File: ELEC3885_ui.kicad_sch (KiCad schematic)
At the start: 0 parts

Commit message: Initial schematic complete
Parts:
- added SW1, SW2, SW3, SW4: SW_Push, Button_Switch_SMD:SW_Push_1P1T_NO_6x6mm_H9.5mm, symbol Switch:SW_Push_Dual
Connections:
- new net BUTTON_0: SW1.1, SW1.3
- new net BUTTON_1: SW2.1, SW2.3
- new net BUTTON_2: SW3.1, SW3.3
- new net BUTTON_3: SW4.1, SW4.3
- new net GND: SW1.2, SW1.4, SW2.2, SW2.4, SW3.2, SW3.4, SW4.2, SW4.4
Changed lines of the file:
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@@
 (kicad_sch (version 20211123) (generator eeschema)
   (paper "A4")
+  (junction (at 154.94 87.63) (diameter 0) (color 0 0 0 0)
+  )
+  (junction (at 154.94 57.15) (diameter 0) (color 0 0 0 0)
+  )
+  (junction (at 154.94 97.79) (diameter 0) (color 0 0 0 0)
+  )
+  (junction (at 137.16 97.79) (diameter 0) (color 0 0 0 0)
+  )
+  (junction (at 154.94 82.55) (diameter 0) (color 0 0 0 0)
+  )
+  (junction (at 137.16 82.55) (diameter 0) (color 0 0 0 0)
+  )
+  (junction (at 154.94 72.39) (diameter 0) (color 0 0 0 0)
+  )
+  (junction (at 154.94 102.87) (diameter 0) (color 0 0 0 0)
+  )
+  (junction (at 154.94 67.31) (diameter 0) (color 0 0 0 0)
+  )
+  (junction (at 137.16 67.31) (diameter 0) (color 0 0 0 0)
+  )
+  (junction (at 137.16 52.07) (diameter 0) (color 0 0 0 0)
+  )
+  (wire (pts (xy 137.16 97.79) (xy 137.16 102.87))
+    (stroke (width 0) (type default) (color 0 0 0 0))
+  )
+  (wire (pts (xy 128.27 82.55) (xy 137.16 82.55))
+    (stroke (width 0) (type default) (color 0 0 0 0))
+  )
+  (wire (pts (xy 137.16 82.55) (xy 137.16 87.63))
+    (stroke (width 0) (type default) (color 0 0 0 0))
+  )
+  (wire (pts (xy 154.94 97.79) (xy 154.94 102.87))
+    (stroke (width 0) (type default) (color 0 0 0 0))
+  )
+  (wire (pts (xy 154.94 67.31) (xy 154.94 72.39))
+    (stroke (width 0) (type default) (color 0 0 0 0))
+  )
+  (wire (pts (xy 128.27 97.79) (xy 137.16 97.79))
+    (stroke (width 0) (type default) (color 0 0 0 0))
+  )
+  (wire (pts (xy 154.94 72.39) (xy 154.94 82.55))
+    (stroke (width 0) (type default) (color 0 0 0 0))
+  )
+  (wire (pts (xy 154.94 52.07) (xy 154.94 57.15))
+    (stroke (width 0) (type default) (color 0 0 0 0))
+  )
+  (wire (pts (xy 154.94 102.87) (xy 147.32 102.87))
+    (stroke (width 0) (type default) (color 0 0 0 0))
+  )
+  (wire (pts (xy 154.94 105.41) (xy 154.94 102.87))
+    (stroke (width 0) (type default) (color 0 0 0 0))
+  )
+  (wire (pts (xy 147.32 52.07) (xy 154.94 52.07))
+    (stroke (width 0) (type default) (color 0 0 0 0))
+  )
+  (wire (pts (xy 147.32 57.15) (xy 154.94 57.15))
+    (stroke (width 0) (type default) (color 0 0 0 0))
+  )
+  (wire (pts (xy 147.32 87.63) (xy 154.94 87.63))
+    (stroke (width 0) (type default) (color 0 0 0 0))
+  )
+  (wire (pts (xy 154.94 57.15) (xy 154.94 67.31))
+    (stroke (width 0) (type default) (color 0 0 0 0))
+  )
+  (wire (pts (xy 147.32 67.31) (xy 154.94 67.31))
+    (stroke (width 0) (type default) (color 0 0 0 0))
+  )
+  (wire (pts (xy 137.16 52.07) (xy 137.16 57.15))
+    (stroke (width 0) (type default) (color 0 0 0 0))
+  )
+  (wire (pts (xy 154.94 87.63) (xy 154.94 97.79))
+    (stroke (width 0) (type default) (color 0 0 0 0))
+  )
+  (wire (pts (xy 128.27 52.07) (xy 137.16 52.07))
+    (stroke (width 0) (type default) (color 0 0 0 0))
+  )
+  (wire (pts (xy 154.94 82.55) (xy 154.94 87.63))
+    (stroke (width 0) (type default) (color 0 0 0 0))
+  )
+  (wire (pts (xy 137.16 67.31) (xy 137.16 72.39))
+    (stroke (width 0) (type default) (color 0 0 0 0))
+  )
+  (wire (pts (xy 147.32 97.79) (xy 154.94 97.79))
+    (stroke (width 0) (type default) (color 0 0 0 0))
+  )
+  (wire (pts (xy 147.32 72.39) (xy 154.94 72.39))
+    (stroke (width 0) (type default) (color 0 0 0 0))
+  )
+  (wire (pts (xy 128.27 67.31) (xy 137.16 67.31))
+    (stroke (width 0) (type default) (color 0 0 0 0))
+  )
+  (wire (pts (xy 147.32 82.55) (xy 154.94 82.55))
+    (stroke (width 0) (type default) (color 0 0 0 0))
+  )
+  (hierarchical_label "BUTTON_2" (shape input) (at 128.27 82.55 180)
+    (effects (font (size 1.27 1.27)) (justify right))
+  )
+  (hierarchical_label "BUTTON_3" (shape input) (at 128.27 97.79 180)
+    (effects (font (size 1.27 1.27)) (justify right))
+  )
+  (hierarchical_label "BUTTON_0" (shape input) (at 128.27 52.07 180)
+    (effects (font (size 1.27 1.27)) (justify right))
+  )
+  (hierarchical_label "BUTTON_1" (shape input) (at 128.27 67.31 180)
+    (effects (font (size 1.27 1.27)) (justify right))
+  )
+  (symbol (lib_id "Switch:SW_Push_Dual") (at 142.24 67.31 0) (unit 1)
+    (in_bom yes) (on_board yes) (fields_autoplaced)
+    (property "Reference" "SW2" (id 0) (at 142.24 59.69 0))
+    (property "Value" "SW_Push" (id 1) (at 142.24 62.23 0))
+    (property "Footprint" "Button_Switch_SMD:SW_Push_1P1T_NO_6x6mm_H9.5mm" (id 2) (at 142.24 62.23 0)
+      (effects (font (size 1.27 1.27)) hide)
+    )
+    (property "Datasheet" "~" (id 3) (at 142.24 62.23 0)
+      (effects (font (size 1.27 1.27)) hide)
+    )
+    (pin "1")
+    (pin "2")
+    (pin "3")
+    (pin "4")
+  )
+  (symbol (lib_id "Switch:SW_Push_Dual") (at 142.24 97.79 0) (unit 1)
+    (in_bom yes) (on_board yes) (fields_autoplaced)
+    (property "Reference" "SW4" (id 0) (at 142.24 90.17 0))
+    (property "Value" "SW_Push" (id 1) (at 142.24 92.71 0))
+    (property "Footprint" "Button_Switch_SMD:SW_Push_1P1T_NO_6x6mm_H9.5mm" (id 2) (at 142.24 92.71 0)
+      (effects (font (size 1.27 1.27)) hide)
+    )
+    (property "Datasheet" "~" (id 3) (at 142.24 92.71 0)
+      (effects (font (size 1.27 1.27)) hide)
+    )
+    (pin "1")
+    (pin "2")
+    (pin "3")
+    (pin "4")
+  )
+  (symbol (lib_id "Switch:SW_Push_Dual") (at 142.24 82.55 0) (unit 1)
+    (in_bom yes) (on_board yes) (fields_autoplaced)
+    (property "Reference" "SW3" (id 0) (at 142.24 74.93 0))
+    (property "Value" "SW_Push" (id 1) (at 142.24 77.47 0))
+    (property "Footprint" "Button_Switch_SMD:SW_Push_1P1T_NO_6x6mm_H9.5mm" (id 2) (at 142.24 77.47 0)
+      (effects (font (size 1.27 1.27)) hide)
+    )
+    (property "Datasheet" "~" (id 3) (at 142.24 77.47 0)
+      (effects (font (size 1.27 1.27)) hide)
+    )
+    (pin "1")
+    (pin "2")
+    (pin "3")
+    (pin "4")
+  )
+  (symbol (lib_id "power:GND") (at 154.94 105.41 0) (unit 1)
+    (in_bom yes) (on_board yes) (fields_autoplaced)
+    (property "Reference" "#PWR0104" (id 0) (at 154.94 111.76 0)
+      (effects (font (size 1.27 1.27)) hide)
+    )
+    (property "Value" "GND" (id 1) (at 154.94 110.49 0))
+    (property "Footprint" "" (id 2) (at 154.94 105.41 0)
+      (effects (font (size 1.27 1.27)) hide)
+    )
+    (property "Datasheet" "" (id 3) (at 154.94 105.41 0)
+      (effects (font (size 1.27 1.27)) hide)
+    )
+    (pin "1")
+  )
+  (symbol (lib_id "Switch:SW_Push_Dual") (at 142.24 52.07 0) (unit 1)
+    (in_bom yes) (on_board yes) (fields_autoplaced)
+    (property "Reference" "SW1" (id 0) (at 142.24 44.45 0))
+    (property "Value" "SW_Push" (id 1) (at 142.24 46.99 0))
+    (property "Footprint" "Button_Switch_SMD:SW_Push_1P1T_NO_6x6mm_H9.5mm" (id 2) (at 142.24 46.99 0)
+      (effects (font (size 1.27 1.27)) hide)
+    )
+    (property "Datasheet" "~" (id 3) (at 142.24 46.99 0)
+      (effects (font (size 1.27 1.27)) hide)
+    )
+    (pin "1")
+    (pin "2")
+    (pin "3")
+    (pin "4")
+  )
 )

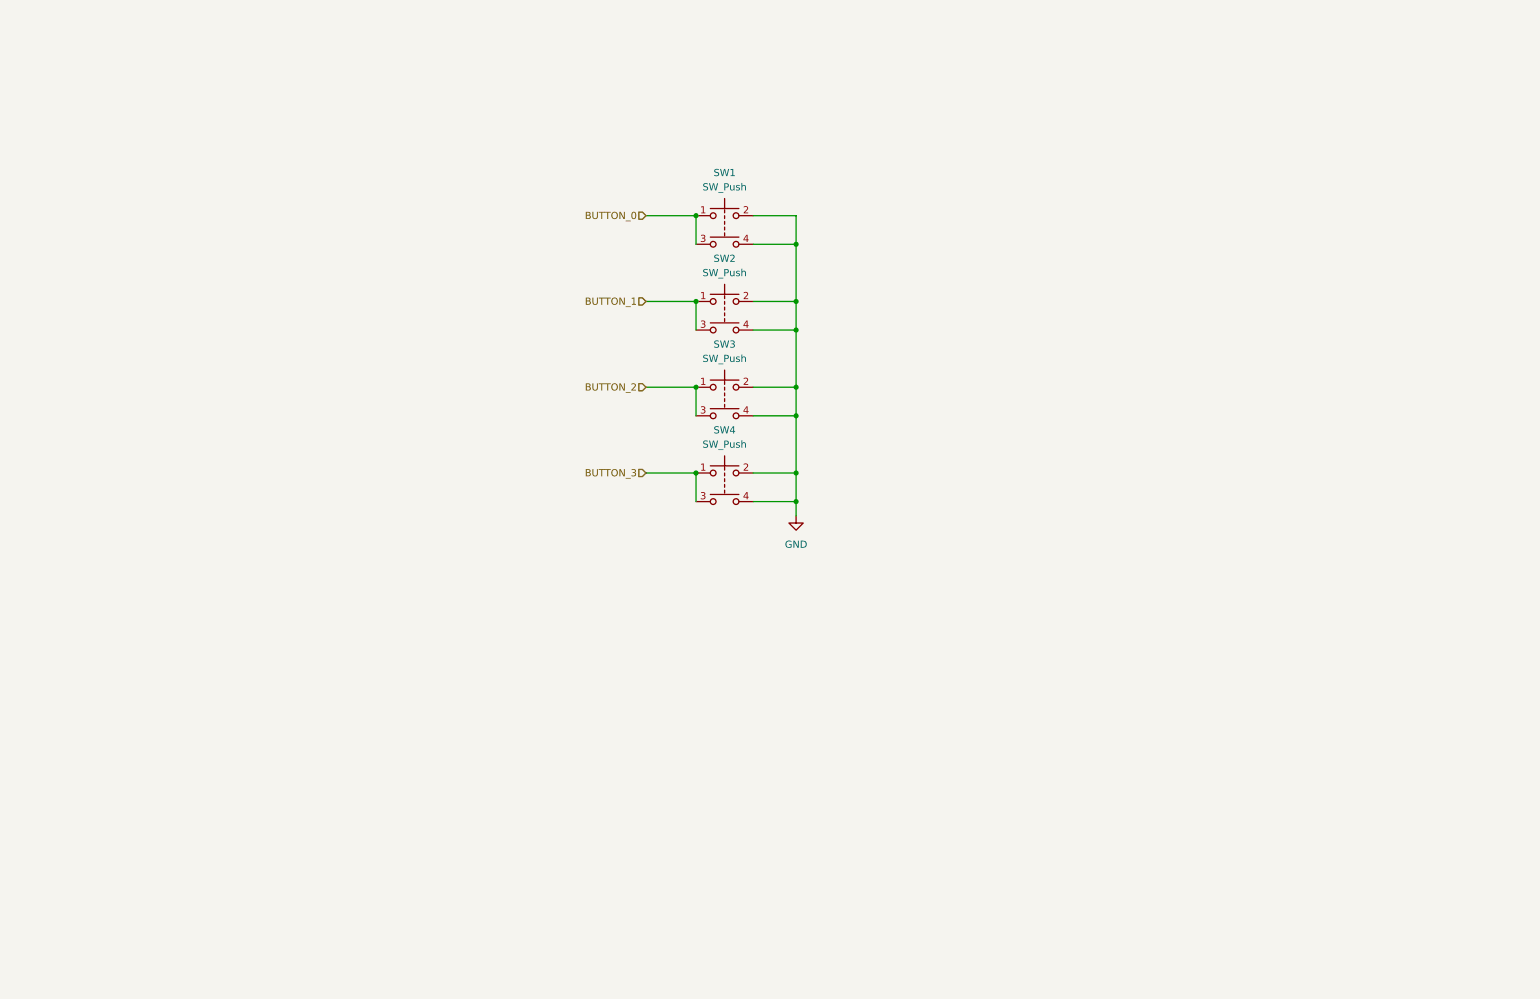
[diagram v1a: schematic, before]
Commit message: Moved to Rev 3, button + LED ui added
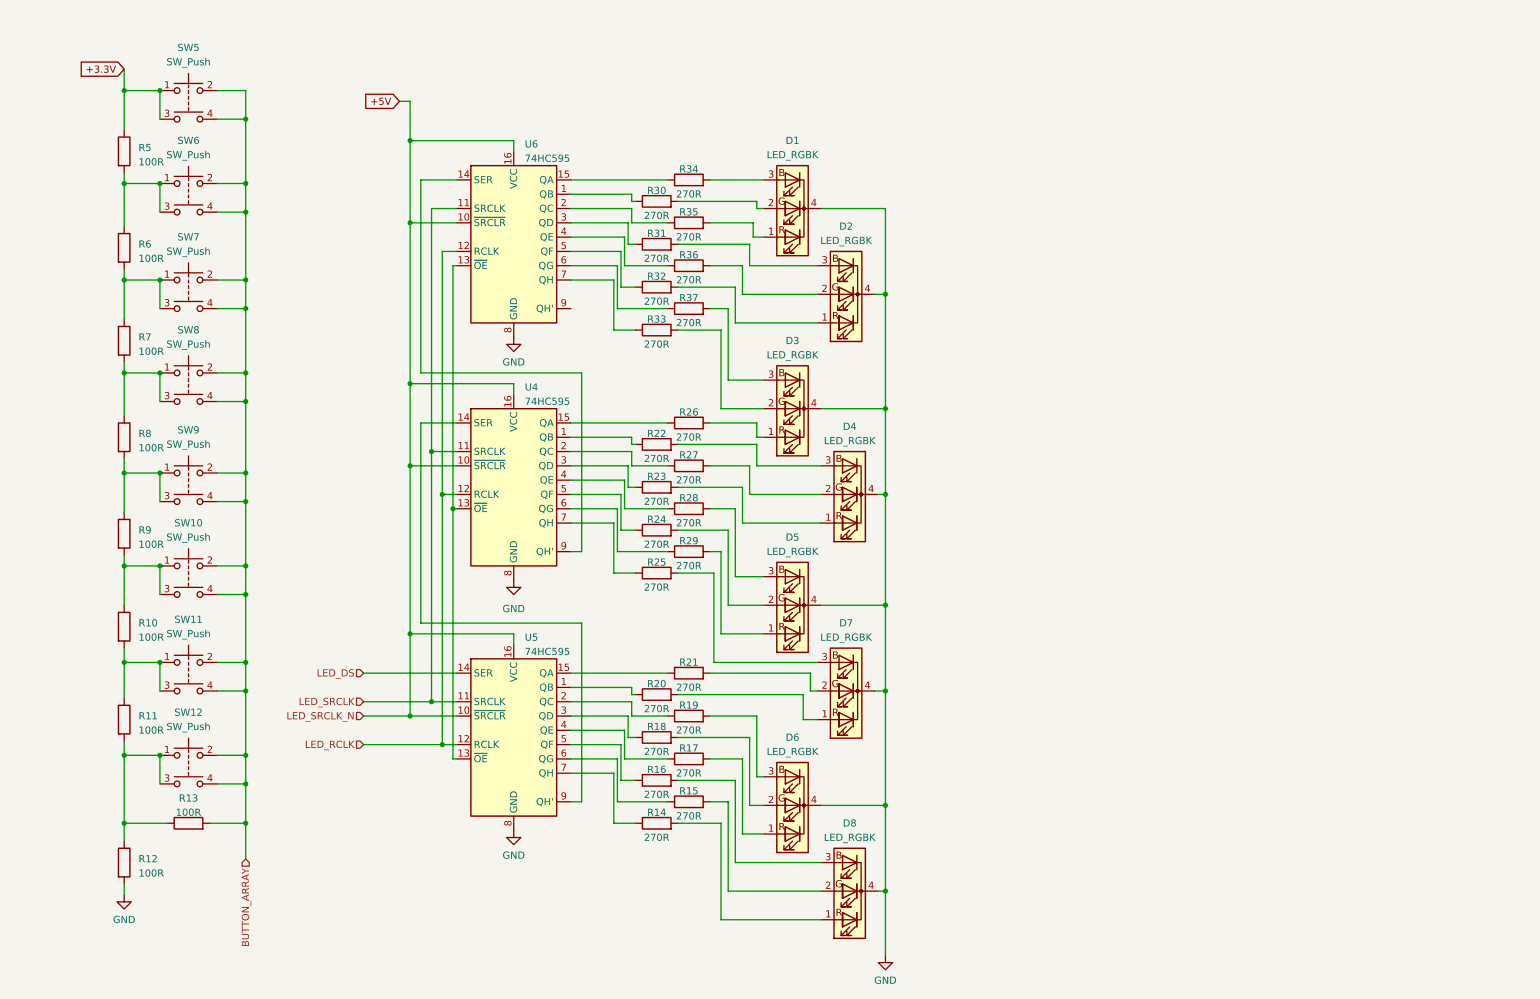
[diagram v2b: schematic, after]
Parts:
- removed SW1, SW2, SW3, SW4: SW_Push, Button_Switch_SMD:SW_Push_1P1T_NO_6x6mm_H9.5mm, symbol Switch:SW_Push_Dual
- added D1, D2, D3, D4, D5, D6, D7, D8: LED_RGBK, symbol Device:LED_RGBK
- added R10, R11, R12, R13, R5, R6, R7, R8, R9: 100R, symbol Device:R
- added R14, R15, R16, R17, R18, R19, R20, R21, R22, R23, R24, R25, R26, R27, R28, R29, R30, R31, R32, R33, R34, R35, R36, R37: 270R, symbol Device:R
- added SW10, SW11, SW12, SW5, SW6, SW7, SW8, SW9: SW_Push, Button_Switch_SMD:SW_Push_1P1T_NO_6x6mm_H9.5mm, symbol Switch:SW_Push_Dual
- added U4, U5, U6: 74HC595, symbol 74xx:74HC595
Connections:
- net GND: now also D1.4 (K), D2.4 (K), D3.4 (K), D4.4 (K), D5.4 (K), D6.4 (K), D7.4 (K), D8.4 (K), R12.2, U4.8 (GND), U5.8 (GND), U6.8 (GND)
- new net: R21.1, U5.15 (QA)
- new net: D7.2 (GA), R21.2
- new net: D6.1 (RA), R17.2
- new net: D6.2 (GA), R18.2
- new net: D6.3 (BA), R19.2
- new net: R11.2, R12.1, R13.1, SW12.1, SW12.3
- new net: R10.2, R11.1, SW11.1, SW11.3
- new net: R5.2, R6.1, SW6.1, SW6.3
- new net: R6.2, R7.1, SW7.1, SW7.3
- new net: R24.1, U4.5 (QF)
- new net: D5.2 (GA), R24.2
- new net: R28.1, U4.4 (QE)
- new net: D5.3 (BA), R28.2
- new net: R10.1, R9.2, SW10.1, SW10.3
- new net: R7.2, R8.1, SW8.1, SW8.3
- new net: R25.1, U4.7 (QH)
- new net: D7.3 (BA), R25.2
- new net: D2.1 (RA), R32.2
- new net: D2.2 (GA), R36.2
- new net: D2.3 (BA), R31.2
- new net: R30.1, U6.1 (QB)
- new net: U4.13 (~{OE}), U5.13 (~{OE}), U6.13 (~{OE})
- new net: U4.9 (QH'), U6.14 (SER)
- new net: R34.1, U6.15 (QA)
- new net: R35.1, U6.2 (QC)
- new net: R31.1, U6.3 (QD)
- new net: R36.1, U6.4 (QE)
- new net: R32.1, U6.5 (QF)
- new net: R37.1, U6.6 (QG)
- new net: R33.1, U6.7 (QH)
- new net: R8.2, R9.1, SW9.1, SW9.3
- new net: D8.1 (RA), R14.2
- new net: D8.2 (GA), R15.2
- new net: D8.3 (BA), R16.2
- new net: D4.1 (RA), R23.2
- new net: D4.2 (GA), R27.2
- new net: D4.3 (BA), R22.2
- new net: R17.1, U5.4 (QE)
- new net: D1.1 (RA), R35.2
- new net: D1.2 (GA), R30.2
- new net: D1.3 (BA), R34.2
- new net: R19.1, U5.2 (QC)
- new net: D3.2 (GA), R33.2
- new net: R22.1, U4.1 (QB)
- new net: U4.14 (SER), U5.9 (QH')
- new net: R26.1, U4.15 (QA)
- new net: R27.1, U4.2 (QC)
- new net: R23.1, U4.3 (QD)
- new net: R29.1, U4.6 (QG)
- new net: R20.1, U5.1 (QB)
- new net: R18.1, U5.3 (QD)
- new net: R16.1, U5.5 (QF)
- new net: R15.1, U5.6 (QG)
- new net: R14.1, U5.7 (QH)
- new net: D3.1 (RA), R26.2
- new net: D3.3 (BA), R37.2
- new net: D7.1 (RA), R20.2
- new net: D5.1 (RA), R29.2
- new net +3.3V: R5.1, SW5.1, SW5.3
- new net +5V: U4.10 (~{SRCLR}), U4.16 (VCC), U5.10 (~{SRCLR}), U5.16 (VCC), U6.10 (~{SRCLR}), U6.16 (VCC)
- new net BUTTON_ARRAY: R13.2, SW10.2, SW10.4, SW11.2, SW11.4, SW12.2, SW12.4, SW5.2, SW5.4, SW6.2, SW6.4, SW7.2, SW7.4, SW8.2, SW8.4, SW9.2, SW9.4
- new net LED_DS: U5.14 (SER)
- new net LED_RCLK: U4.12 (RCLK), U5.12 (RCLK), U6.12 (RCLK)
- new net LED_SRCLK: U4.11 (SRCLK), U5.11 (SRCLK), U6.11 (SRCLK)

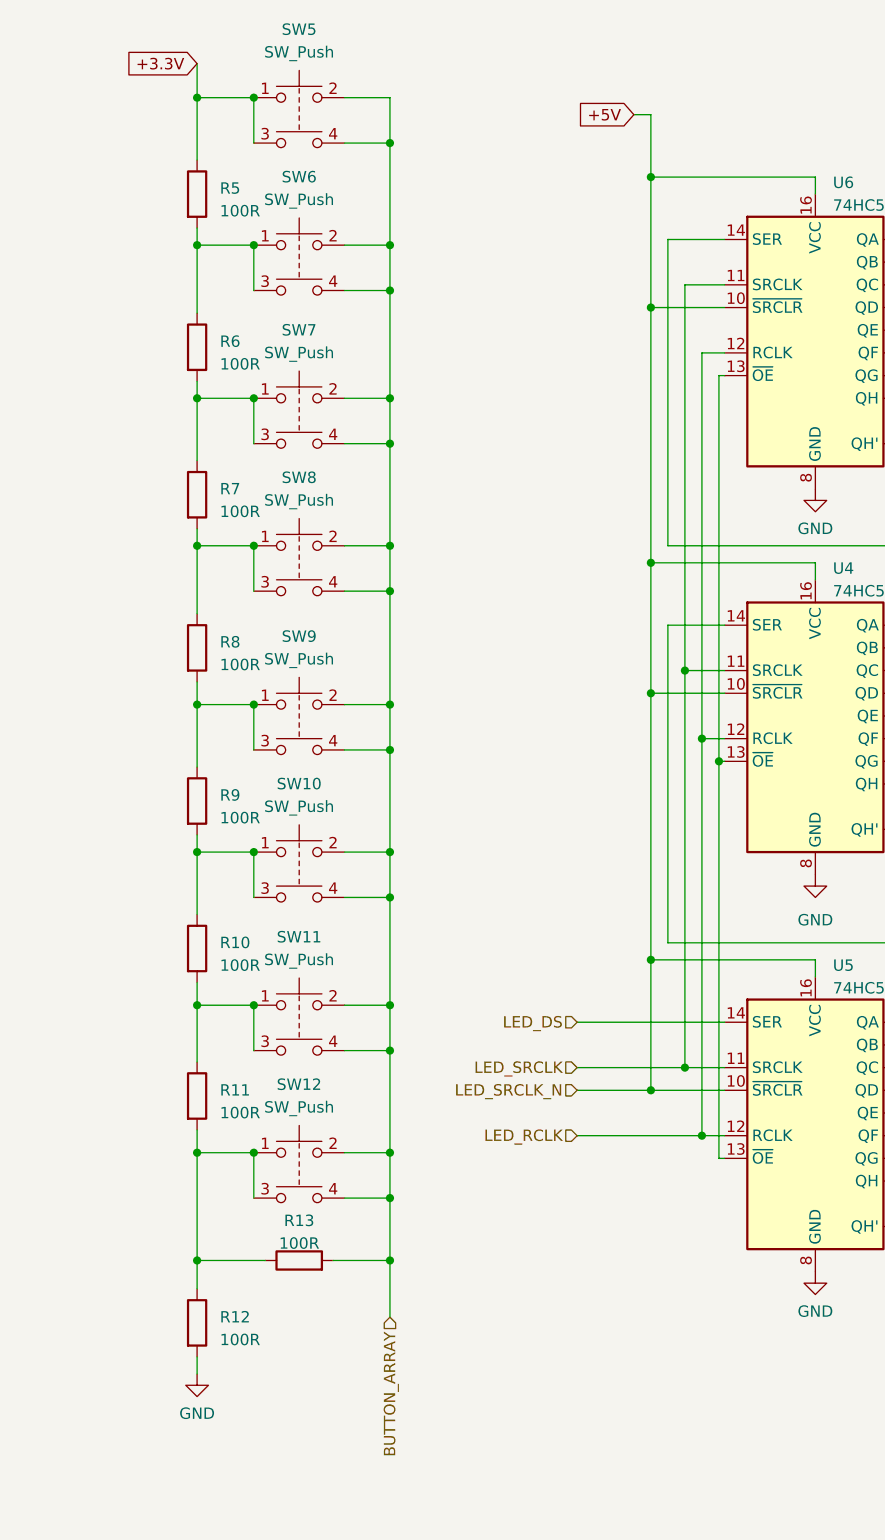
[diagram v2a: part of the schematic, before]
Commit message: UI testpoints added
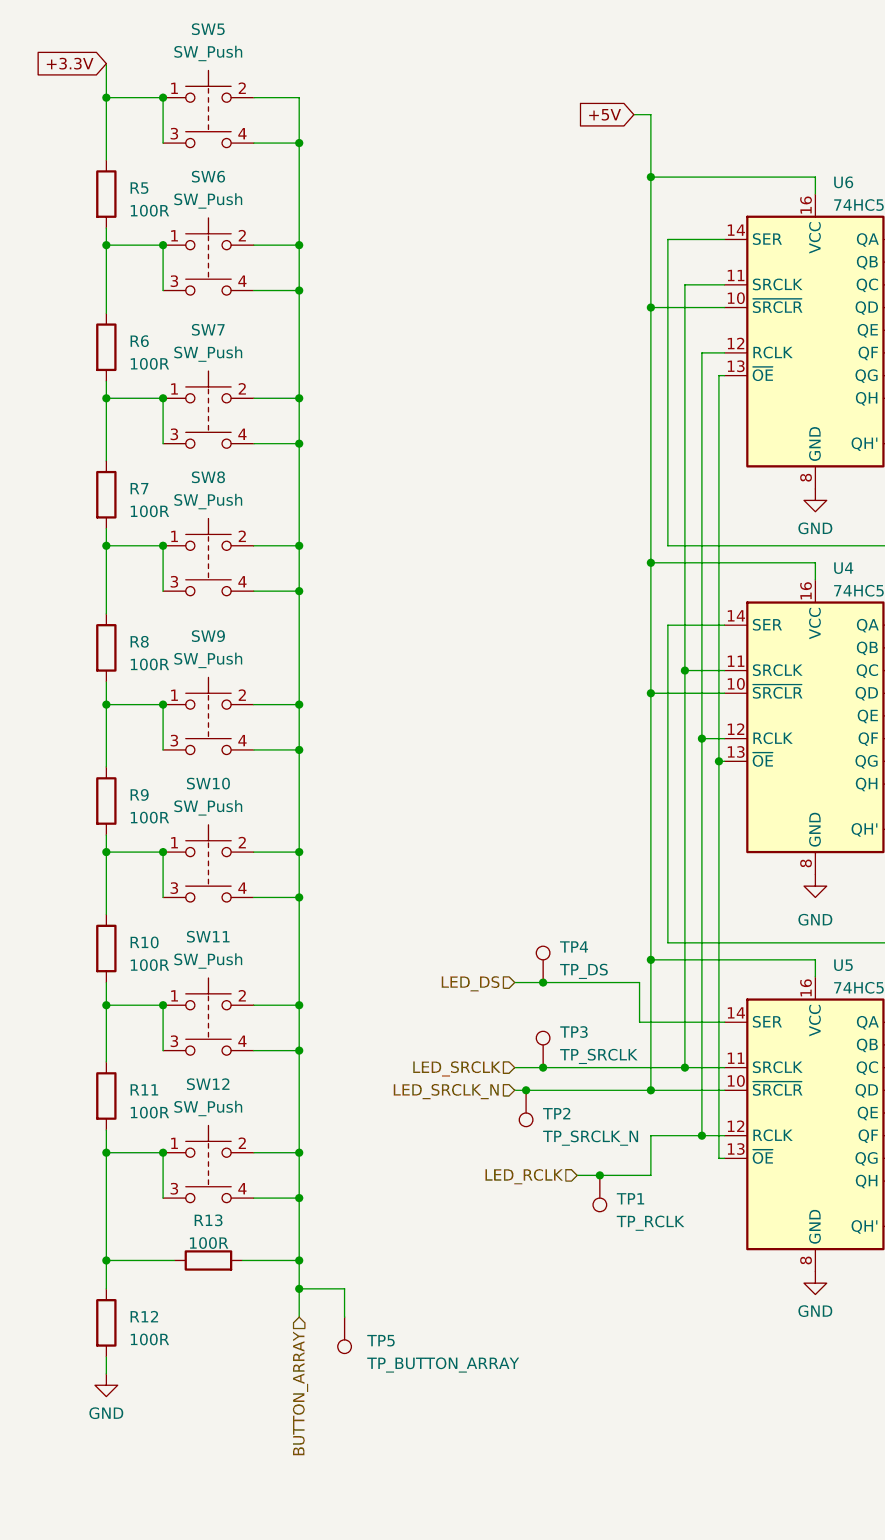
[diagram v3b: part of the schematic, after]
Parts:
- added TP1: TP_RCLK, symbol Connector:TestPoint
- added TP2: TP_SRCLK_N, symbol Connector:TestPoint
- added TP3: TP_SRCLK, symbol Connector:TestPoint
- added TP4: TP_DS, symbol Connector:TestPoint
- added TP5: TP_BUTTON_ARRAY, symbol Connector:TestPoint
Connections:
- net +5V: now also TP2.1
- net BUTTON_ARRAY: now also TP5.1
- net LED_DS: now also TP4.1
- net LED_RCLK: now also TP1.1
- net LED_SRCLK: now also TP3.1
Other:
- moved on the sheet: R10, R11, R12, R13, R5, R6, R7, R8, R9, SW10, SW11, SW12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
